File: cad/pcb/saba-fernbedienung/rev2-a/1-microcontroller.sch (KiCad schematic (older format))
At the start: 15 parts, among them J201 Conn_ARM_JTAG_SWD_10, U201 DOIT-DEVKITV1-ESP32-WROOM-32, U202 LTV-357T

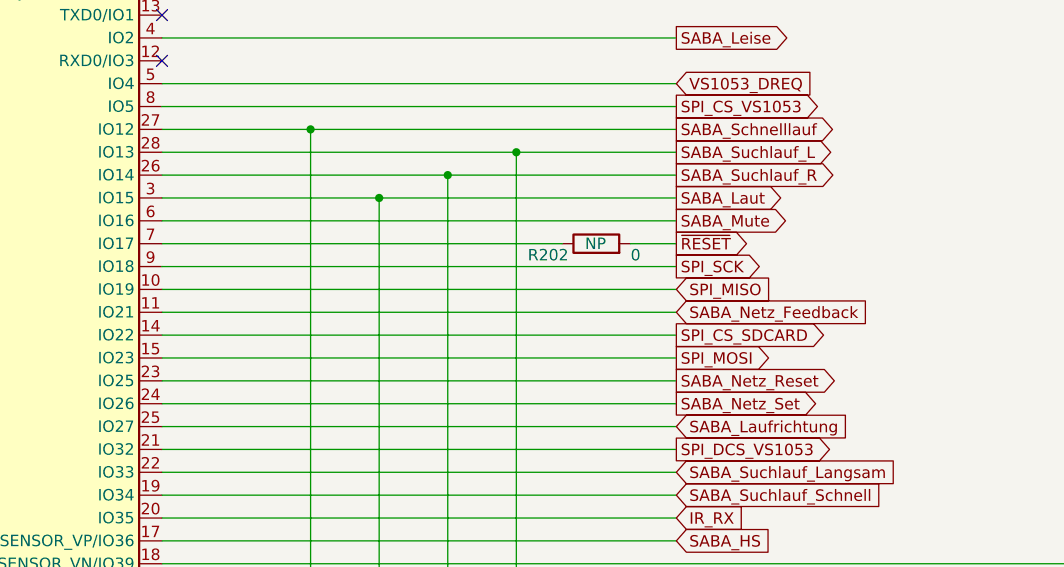
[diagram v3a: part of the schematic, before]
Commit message: alle Bauteile platziert
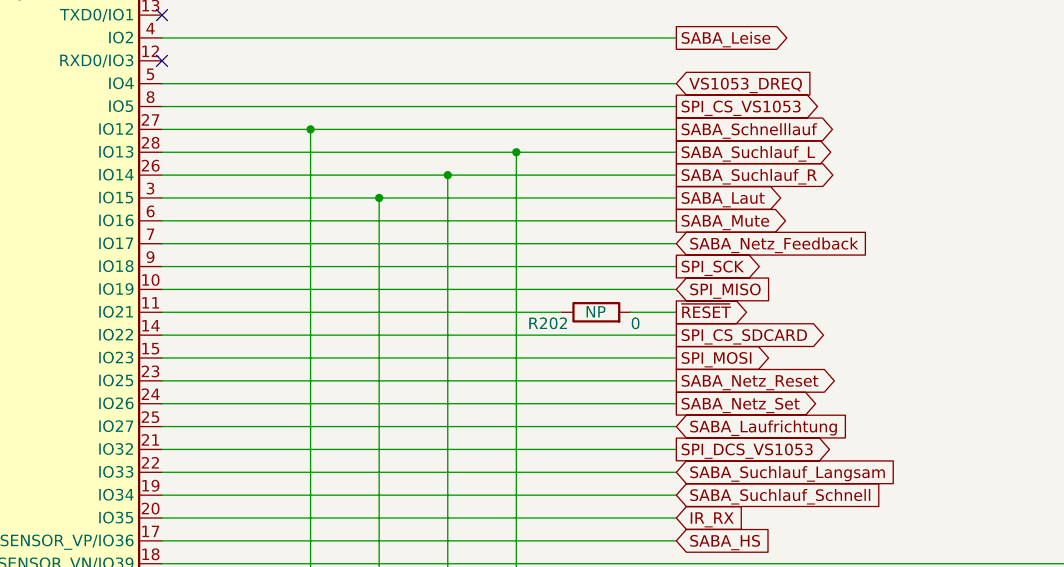
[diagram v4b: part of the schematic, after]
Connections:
- net SABA_Netz_Feedback: now also U201.7 (IO17); no longer U201.11 (IO21)
- net at R202.1: now also U201.11 (IO21); no longer U201.7 (IO17)
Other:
- moved on the sheet: R202
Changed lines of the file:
@@
 Text GLabel 5550 3400 2    50   Output ~ 0
 SABA_Netz_Reset
-Text GLabel 5550 3100 2    50   Input ~ 0
+Text GLabel 5550 2800 2    50   Input ~ 0
 SABA_Netz_Feedback
 Wire Wire Line
-	5550 3100 3300 3100
-Wire Wire Line
 	1650 1900 1450 1900
-Text GLabel 5550 2800 2    50   Output ~ 0
+Text GLabel 5550 3100 2    50   Output ~ 0
 ~RESET
 $Comp
@@
 L Device:R R202
 U 1 1 61303F4D
-P 5200 2800
-F 0 "R202" V 5150 3100 50  0000 R CNN
-F 1 "0" V 5150 2650 50  0000 R CNN
-F 2 "Resistor_SMD:R_0603_1608Metric" V 5130 2800 50  0001 C CNN
-F 3 "~" H 5200 2800 50  0001 C CNN
-F 4 "NP" V 5200 2850 50  0000 R CNN "Placement"
-	1    5200 2800
+P 5200 3100
+F 0 "R202" V 5150 3400 50  0000 R CNN
+F 1 "0" V 5150 2950 50  0000 R CNN
+F 2 "Resistor_SMD:R_0603_1608Metric" V 5130 3100 50  0001 C CNN
+F 3 "~" H 5200 3100 50  0001 C CNN
+F 4 "NP" V 5200 3150 50  0000 R CNN "Placement"
+	1    5200 3100
 	0    -1   -1   0
 $EndComp
-Wire Wire Line
-	5550 2800 5350 2800
-Wire Wire Line
-	5050 2800 3300 2800
 $Comp
 L Device:D D?
@@
 Wire Wire Line
 	9900 4200 10100 4200
+Wire Wire Line
+	3300 2800 5550 2800
+Wire Wire Line
+	5550 3100 5350 3100
+Wire Wire Line
+	5050 3100 3300 3100
 $EndSCHEMATC
